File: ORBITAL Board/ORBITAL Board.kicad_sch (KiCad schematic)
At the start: 94 parts, among them J1 Conn_01x02, J2 Micro_SD_Card_Det, J3 Conn_01x12, J4 Conn_01x12, P1 USB_C_Plug_USB2.0, SW1 SW_DPST_x2, U1 PTPS563206DRLR, U2 W25Q128JVS, U3 USBLC6-2SC6, U4 LTC3118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

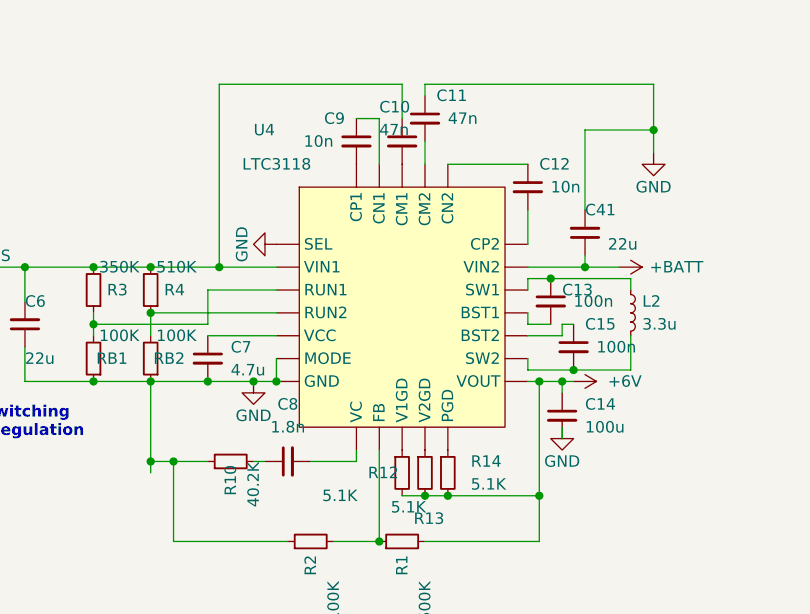
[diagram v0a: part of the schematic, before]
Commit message: Adding in LTC3118 to PCB
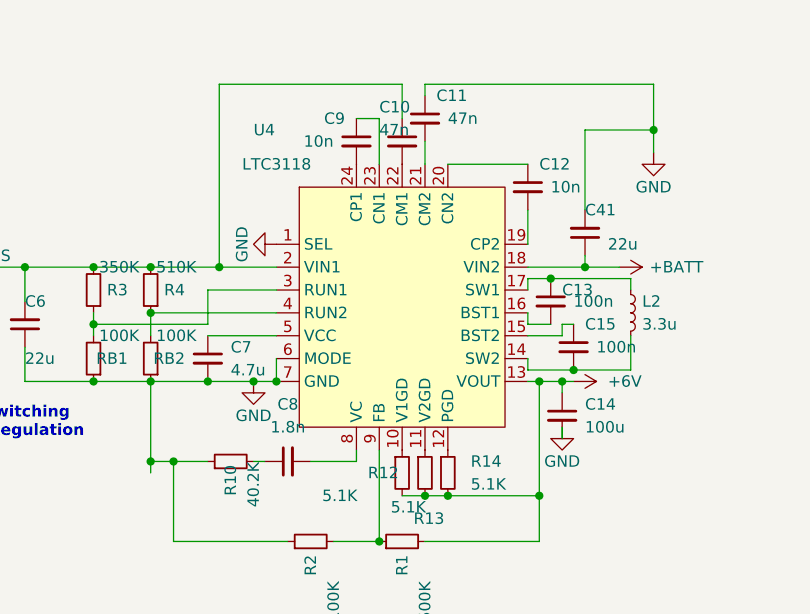
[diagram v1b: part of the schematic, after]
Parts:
- U4: footprint (none) -> DCDC Converters:LTC3118
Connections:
- net +6V: now also U4.13 (VOUT); no longer U4. (VOUT)
- net +BATT: now also U4.18 (VIN2); no longer U4. (VOUT)
- net GND: now also U4.1 (SEL), U4.6 (MODE), U4.7 (GND); no longer U4. (VOUT)
- net VBUS: now also U4.2 (VIN1); no longer U4. (VOUT)
- net at R1.1, R2.2: now also U4.9 (FB); no longer U4. (VOUT)
- net at C7.1: now also U4.5 (VCC); no longer U4. (VOUT)
- net at C13.1, L2.1: now also U4.17 (SW1); no longer U4. (VOUT)
- net at C15.2, L2.2: now also U4.14 (SW2); no longer U4. (VOUT)
- net at C11.2: now also U4.21 (CM2); no longer U4. (VOUT)
- net at R3.1, RB1.2: now also U4.3 (RUN1); no longer U4. (VOUT)
- net at R4.1, RB2.2: now also U4.4 (RUN2); no longer U4. (VOUT)
- net at C12.1: now also U4.20 (CN2); no longer U4. (VOUT)
- net at C12.2: now also U4.19 (CP2); no longer U4. (VOUT)
- net at C13.2: now also U4.16 (BST1); no longer U4. (VOUT)
- net at R13.1: now also U4.11 (V2GD); no longer U4. (VOUT)
- net at R14.1: now also U4.12 (PGD); no longer U4. (VOUT)
- net at C15.1: now also U4.15 (BST2); no longer U4. (VOUT)
- net at C8.2: now also U4.8 (VC); no longer U4. (VOUT)
- net at R12.1: now also U4.10 (V1GD); no longer U4. (VOUT)
- net at C10.2: now also U4.22 (CM1); no longer U4. (VOUT)
- net at C9.1: now also U4.23 (CN1); no longer U4. (VOUT)
- net at C9.2: now also U4.24 (CP1); no longer U4. (VOUT)
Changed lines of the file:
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@@
       (effects (font (size 1.27 1.27)) (justify left))
     )
-    (property "Footprint" "" (at 157.48 53.34 0)
+    (property "Footprint" "DCDC Converters:LTC3118" (at 157.48 53.34 0)
       (effects (font (size 1.27 1.27)) hide)
     )
@@
       (effects (font (size 1.27 1.27)) hide)
     )
-    (pin "")
-    (pin "")
-    (pin "")
-    (pin "")
-    (pin "")
-    (pin "")
-    (pin "")
-    (pin "")
-    (pin "")
-    (pin "")
-    (pin "")
-    (pin "")
-    (pin "")
-    (pin "")
-    (pin "")
-    (pin "")
-    (pin "")
-    (pin "")
-    (pin "")
-    (pin "")
-    (pin "")
-    (pin "")
-    (pin "")
-    (pin "")
+    (pin "2")
+    (pin "9")
+    (pin "10")
+    (pin "18")
+    (pin "24")
+    (pin "23")
+    (pin "17")
+    (pin "7")
+    (pin "5")
+    (pin "15")
+    (pin "13")
+    (pin "19")
+    (pin "12")
+    (pin "1")
+    (pin "4")
+    (pin "11")
+    (pin "6")
+    (pin "16")
+    (pin "21")
+    (pin "20")
+    (pin "3")
+    (pin "22")
+    (pin "8")
+    (pin "14")
     (instances
       (project "ORBITAL Board"
